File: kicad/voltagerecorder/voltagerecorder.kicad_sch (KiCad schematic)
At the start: 84 parts, among them J1 Conn_02x10_Odd_Even, J3 Conn_01x08, P1 DM3CS-SF, U1 Opamp_Quad, U5 ADS8638, U8 ESP32-C3-WROOM-02

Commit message: Pinout mit Viktor abgesprochen.
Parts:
- removed C38: 100n, Capacitor_SMD:C_0603_1608Metric_Pad1.08x0.95mm_HandSolder, symbol Device:C
- removed C? (x6): 100nF, Capacitor_SMD:C_0603_1608Metric, symbol Device:C
- removed C? (x2): 1uF, Capacitor_SMD:C_0603_1608Metric, symbol Device:C
- removed C?: 4.7uF, Capacitor_SMD:C_0603_1608Metric, symbol Device:C
- removed D?: D_Schottky, Diode_SMD:D_0603_1608Metric_Pad1.05x0.95mm_HandSolder, symbol Device:D_Schottky
- removed D?: YELLOW, Diode_SMD:D_0603_1608Metric, symbol Device:LED_Filled
- removed FB?: 220R / 100MHz, Inductor_SMD:L_0603_1608Metric_Pad1.05x0.95mm_HandSolder, symbol Device:FerriteBead
- removed J?: Conn_01x06, symbol Connector_Generic:Conn_01x06
- removed J?: Conn_01x02, Connector_PinHeader_2.54mm:PinHeader_1x02_P2.54mm_Vertical, symbol Connector_Generic:Conn_01x02
- removed R39: 10k, Resistor_SMD:R_0603_1608Metric_Pad0.98x0.95mm_HandSolder, symbol Device:R
- removed R40: 15k, Resistor_SMD:R_0603_1608Metric_Pad0.98x0.95mm_HandSolder, symbol Device:R
- removed R? (x2): 1k, Resistor_SMD:R_0603_1608Metric_Pad0.98x0.95mm_HandSolder, symbol Device:R
- removed R?: 1k, Resistor_SMD:R_0603_1608Metric, symbol Device:R
- removed R? (x2): 10k, Resistor_SMD:R_0603_1608Metric, symbol Device:R
- removed R?: 3k3, Resistor_SMD:R_0603_1608Metric_Pad0.98x0.95mm_HandSolder, symbol Device:R
- added BT1: Battery_Cell, symbol Device:Battery_Cell
- added C24, C29, C30, C32, C39, C45: 100n, Capacitor_SMD:C_0603_1608Metric_Pad1.08x0.95mm_HandSolder, symbol Device:C
- added C31: 1u, Capacitor_SMD:C_0603_1608Metric_Pad1.08x0.95mm_HandSolder, symbol Device:C
- added C41, C42: 22pF, Capacitor_SMD:C_0603_1608Metric, symbol Device:C
- added D10, D11, D12, D5, D6, D7, D8: D_Zener, symbol Device:D_Zener
- added J10: Conn_01x02, Connector_PinHeader_2.54mm:PinHeader_1x02_P2.54mm_Vertical, symbol Connector_Generic:Conn_01x02
- added J?: Conn_02x03_Odd_Even, symbol Connector_Generic:Conn_02x03_Odd_Even
- added J?: Conn_01x05, symbol Connector_Generic:Conn_01x05
- added R3, R32, R37: 10k, Resistor_SMD:R_0603_1608Metric_Pad0.98x0.95mm_HandSolder, symbol Device:R
- added R41: 15k, Resistor_SMD:R_0603_1608Metric_Pad0.98x0.95mm_HandSolder, symbol Device:R
- added Y1: 32.768kHz, Crystal:Crystal_SMD_3225-4Pin_3.2x2.5mm, symbol Device:Crystal_GND24
- R47: renamed from R?; value 3k3 -> 10k
- gave numbers to parts that had none: 27
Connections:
- net USB_CC1 is gone; now on net USB_CC: J11.A5 (CC1), J12.A5 (CC1)
- net USB_CC2 is gone; now on net USB_CC: J11.B5 (CC2), J12.B5 (CC2), R47.1
- net VDDA is gone; now on net +3.3V: U6.21 (VDDA)
- net +3.3V: now also U6.24 (VDD), U6.36 (VDD), U6.48 (VDD), C24.1, C29.1, C30.1, J?.2 (Pin_2), R32.2
- net +5V: now also J10.2 (Pin_2), R37.2
- net 3V3: no longer U6.1 (VBAT), U6.24 (VDD), U6.36 (VDD), U6.48 (VDD)
- net AL_PD: no longer U5.22 (AL_PD)
- net BOOT0: now also R3.2
- net ESP_BOOT: now also J?.2 (Pin_2)
- net ESP_EN: now also U6.9 (PA1), J?.1 (Pin_1)
- net G4_NRST: now also C32.1, R32.1
- net GND: now also BT1.2 (-), C24.2, C29.2, C30.2, C31.2, C32.2, C39.2, C41.2, C42.2, C45.2, D10.2 (A), D11.2 (A), D12.2 (A), D5.2 (A), D6.2 (A), D7.2 (A), D8.2 (A), J?.1 (Pin_1), J?.5 (Pin_5), R3.1, R41.1, Y1.2, Y1.4
- net LED-GREEN: no longer U6.16 (PB0)
- net LED-RED: no longer U6.18 (PB2)
- net SPI2_MISO: now also R1.2; no longer U9.2 (SO/SIO)
- net SPI2_MOSI: now also U5.18 (DIN); no longer U9.5 (SI/SIO)
- net SPI2_NSS: now also R2.1, U5.16 (CS); no longer U9.1 (~{CE})
- net SPI3_MISO: now also D7.1 (K)
- net SPI3_MOSI: now also D5.1 (K)
- net SPI3_NSS: now also D8.1 (K)
- net UART_G4RX_ESPTX: now also U6.25 (PB11), J?.3 (Pin_3)
- net UART_G4TX_ESPRX: now also U6.22 (PB10), J?.4 (Pin_4)
- net USB-D+: now also D12.1 (K); no longer J12.A6 (D+), J12.B6 (D+)
- net USB-D-: now also D11.1 (K); no longer J12.A7 (D-), J12.B7 (D-)
- net at J11.A4 (VBUS), J11.A9 (VBUS), J11.B4 (VBUS)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: now also J10.1 (Pin_1)
- net QSPI_IO2: now reaches U9.3 (SIO2)
- net QSPI_IO2: now also U6.15 (PA7)
- net QSPI_IO3: now reaches U9.7 (SIO3)
- net QSPI_IO3: now also U6.14 (PA6)
- net QSPI_NSS: now reaches U6.10 (PA2)
- net QSPI_NSS: now also U9.1 (~{CE})
- net QSPI_CLK: now reaches U6.11 (PA3)
- net QSPI_CLK: now also U9.6 (SCLK)
- net ADC_PD: now reaches U6.30 (PA8)
- net ADC_PD: now also U5.22 (AL_PD)
- net USB_CC: now reaches U6.43 (PB6)
- net USB_CC: now also D10.1 (K)
- net LED_RED: now reaches U6.44 (PB7)
- net LED_GREEN: now reaches U6.46 (PB9)
- net PA0: now reaches U6.8 (PA0)
- net PA0: now also J?.3 (Pin_3)
- net 3V3-EN: no longer names the net of U6.2 (PC13)
- net 3V3-FAULT: no longer names the net of U6.4 (PC15-OSC32_OUT)
- net 3V3-FAULT: now also C42.1, Y1.3
- net 5V-FAULT: no longer names the net of U6.3 (PC14-OSC32_IN)
- net 5V-FAULT: now also C41.1, Y1.1
- net LED-YELLOW renamed QSPI_IO0
- net QSPI_IO0: now also U9.2 (SO/SIO)
- removed net SPI1_MISO: R1.2, U6.14 (PA6)
- removed net SPI1_MOSI: U5.18 (DIN), U6.15 (PA7)
- removed net SPI1_NSS: R2.1, U5.16 (CS), U6.12 (PA4)
- net SPI1_SCK renamed PA5
- net PA5: now also J?.6 (Pin_6); no longer U5.17 (SCLK)
- net SPI2_SCK renamed SPI2_CLK
- net SPI2_CLK: now also U5.17 (SCLK); no longer U9.6 (SCLK)
- net SPI3_SCK renamed SPI3_CLK
- net SPI3_CLK: now also D6.1 (K)
- net VREF+: no longer names the net of U6.20 (VREF+)
- net VREF+: now also C31.1, C39.1
- new net: BT1.1 (+), U6.1 (VBAT)
- new net PA4: J?.4 (Pin_4), U6.12 (PA4)
- new net QSPI_IO1: U6.16 (PB0), U9.5 (SI/SIO)
- new net SENSE_5V: C45.1, R37.1, R41.2, U6.18 (PB2)
- no-connect marks 0 -> 3
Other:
- note added: "ADC2_IN12"
- note added: "DAC1_OUT1"
- note added: "DAC1_OUT2"
- note added: "DAC2_OUT1"
- note added: "Power down: low active internal pull up"
- note added: "TVS Dioden 3.3V unidir"
- note added: "TVS Dioden 3.3V unidir 15pF ist ok"
- note added: "TVS Dioden 5V unidir"
- note added: "USART1_RX"
- note added: "USART1_TX"
- note added: "für G4"
- note removed: "AL_PD"
- note removed: "AL_PD: low active internal pull up"
- note removed: "PA10"
- note removed: "PA9"
- note removed: "PB4"
- note removed: "PB6"
- note removed: "SENSE_+5V"
- note removed: "TVS Dioden 3.3V working voltage gegen GND."
- note removed: "TVS Dioden 3.3V working voltage gegen GND. 15pF ist ok."
- note removed: "Trigger in and out"
- note removed: "WOFÜR DIE FAULT PINS??"
- moved on the sheet: C1, C26, C28, C3, C36, C37, C40, C43, C44, C46, C47, D14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

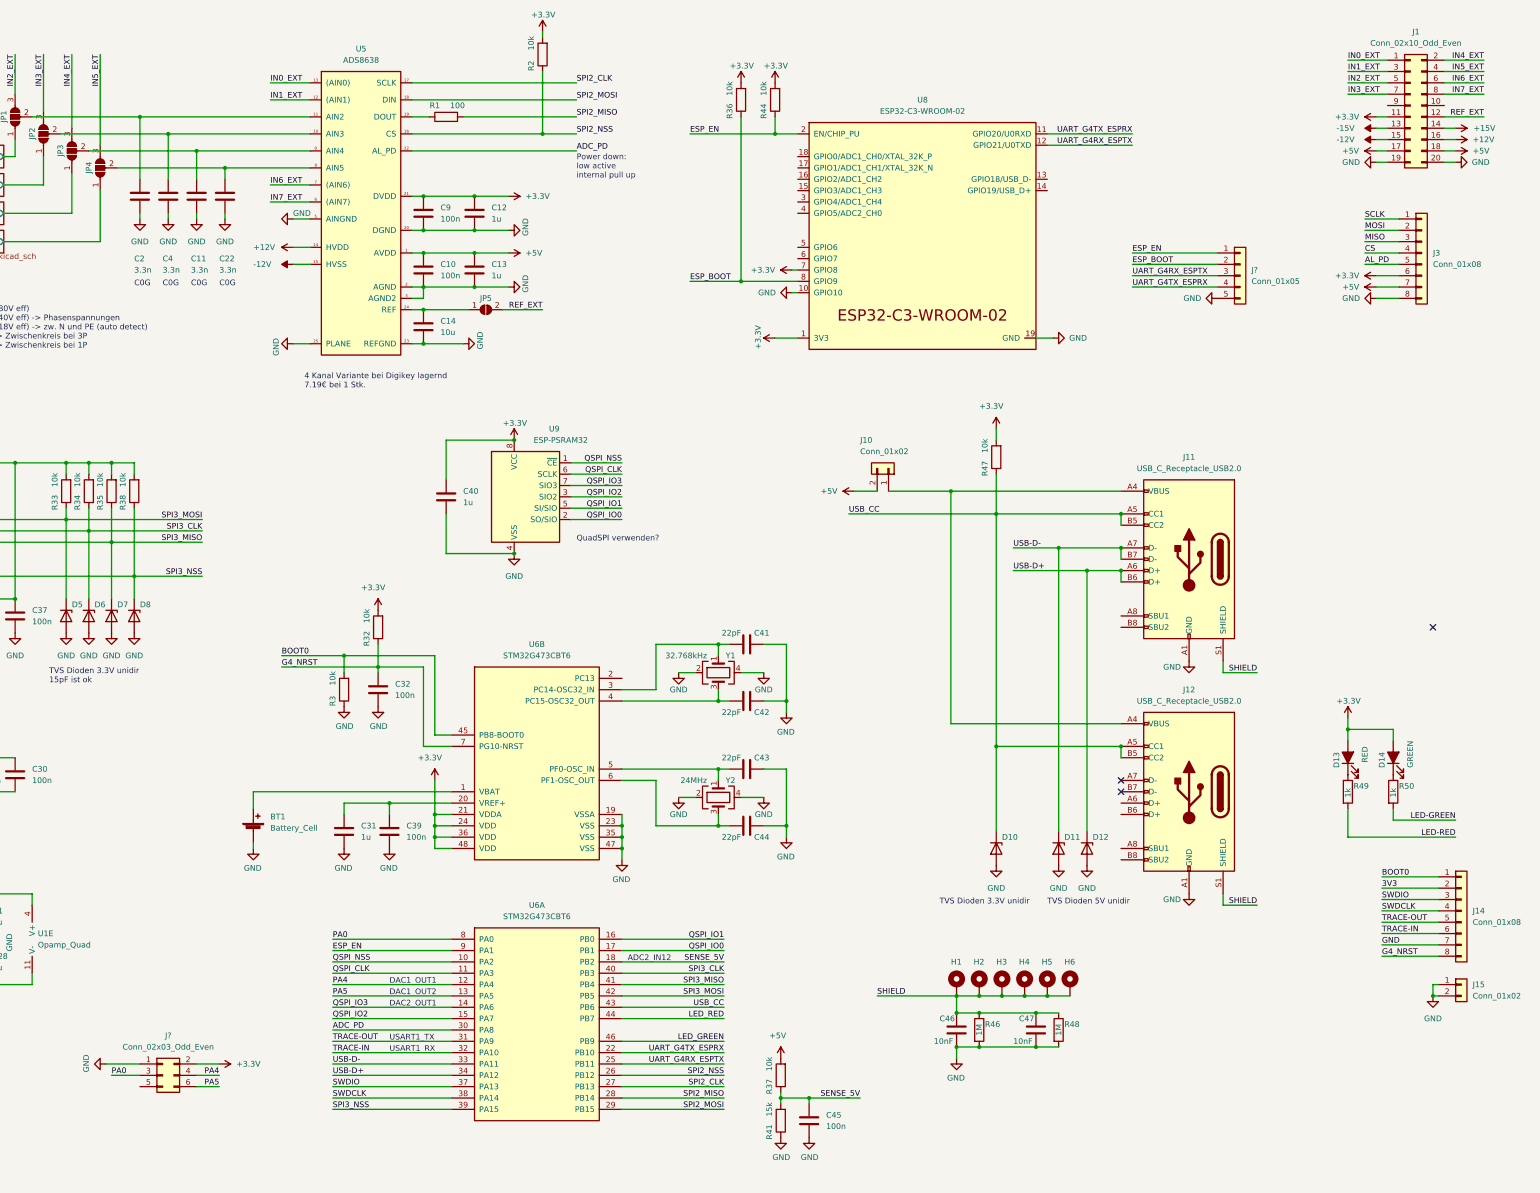
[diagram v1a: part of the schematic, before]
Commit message: Packages zugeordnet, bom ergänzt.
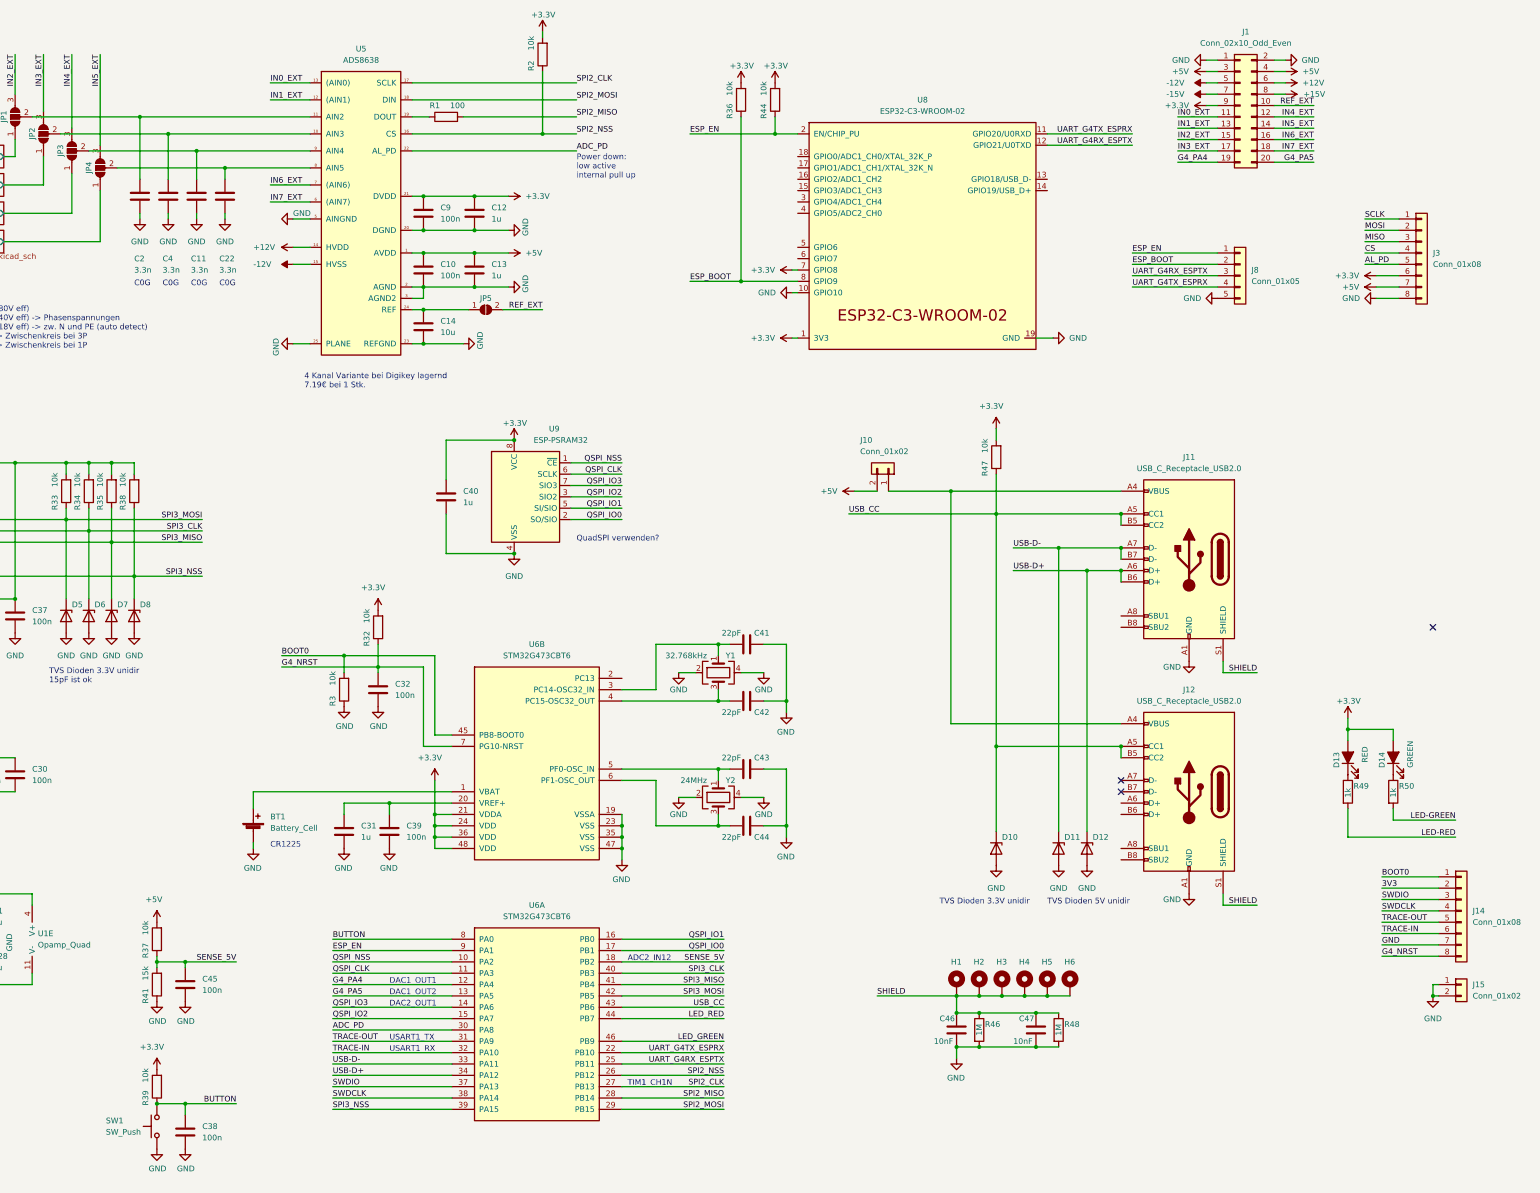
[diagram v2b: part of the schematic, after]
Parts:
- removed J?: Conn_02x03_Odd_Even, symbol Connector_Generic:Conn_02x03_Odd_Even
- added C38: 100n, Capacitor_SMD:C_0603_1608Metric_Pad1.08x0.95mm_HandSolder, symbol Device:C
- added R39: 10k, Resistor_SMD:R_0603_1608Metric_Pad0.98x0.95mm_HandSolder, symbol Device:R
- added SW1: SW_Push, Button_Switch_SMD:SW_Tactile_SPST_NO_Straight_CK_PTS636Sx25SMTRLFS, symbol Switch:SW_Push
- BT1: footprint (none) -> Battery:BatteryHolder_Keystone_500
- C41, C42, C43, C44, C46, C47: footprint Capacitor_SMD:C_0603_1608Metric -> Capacitor_SMD:C_0603_1608Metric_Pad1.08x0.95mm_HandSolder
- D10, D11, D12, D5, D6, D7, D8: footprint (none) -> Diode_SMD:D_SOD-323_HandSoldering
- J8: renamed from J?; footprint (none) -> Connector_PinHeader_2.54mm:PinHeader_1x05_P2.54mm_Vertical
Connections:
- net +12V: now also J1.6 (Pin_6); no longer J1.16 (Pin_16)
- net +15V: now also J1.8 (Pin_8); no longer J1.14 (Pin_14)
- net +3.3V: now also J1.9 (Pin_9), R39.2; no longer J1.11 (Pin_11)
- net +5V: now also J1.3 (Pin_3), J1.4 (Pin_4); no longer J1.17 (Pin_17), J1.18 (Pin_18)
- net -12V: now also J1.5 (Pin_5); no longer J1.15 (Pin_15)
- net -15V: now also J1.7 (Pin_7); no longer J1.13 (Pin_13)
- net GND: now also J1.1 (Pin_1), J1.2 (Pin_2), C38.2, SW1.1; no longer J1.19 (Pin_19), J1.20 (Pin_20)
- net IN0_EXT: now also J1.11 (Pin_11); no longer J1.1 (Pin_1)
- net IN1_EXT: now also J1.13 (Pin_13); no longer J1.3 (Pin_3)
- net IN2_EXT: now also J1.15 (Pin_15); no longer J1.5 (Pin_5)
- net IN3_EXT: now also J1.17 (Pin_17); no longer J1.7 (Pin_7)
- net IN4_EXT: now also J1.12 (Pin_12); no longer J1.2 (Pin_2)
- net IN5_EXT: now also J1.14 (Pin_14); no longer J1.4 (Pin_4)
- net IN6_EXT: now also J1.16 (Pin_16); no longer J1.6 (Pin_6)
- net IN7_EXT: now also J1.18 (Pin_18); no longer J1.8 (Pin_8)
- net REF_EXT: now also J1.10 (Pin_10); no longer J1.12 (Pin_12)
- net PA0 renamed BUTTON
- net BUTTON: now also C38.1, R39.1, SW1.2
- net PA4 renamed G4_PA4
- net G4_PA4: now also J1.19 (Pin_19)
- net PA5 renamed G4_PA5
- net G4_PA5: now also J1.20 (Pin_20)
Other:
- note added: "CR1225"
- note added: "TIM1_CH1N"
- moved on the sheet: C45, R37, R41
